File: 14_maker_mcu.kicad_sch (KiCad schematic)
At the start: 13 parts, among them J900 Maker MCU module socket, Pico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, J901 Exposed maker GPIO/power head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, J902 Maker SWD/debug header, SW900 Maker reset/RUN, SW901 Maker boot/user, U900 USBLC6-2P6 maker USB ESD

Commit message: Publish the current Ducktop2 design
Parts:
- added C902: 4.7u flash bulk, Capacitor_SMD:C_0402_1005Metric, symbol Device:C
- added C903: 100n flash local, Capacitor_SMD:C_0402_1005Metric, symbol Device:C
- added C904, C905, C906, C907, C908, C909, C910: 100n RP2350 3V3 local, Capacitor_SMD:C_0402_1005Metric, symbol Device:C
- added C911: 4.7u VREG input, Capacitor_SMD:C_0402_1005Metric, symbol Device:C
- added C912: 4.7u 1V1 output, Capacitor_SMD:C_0402_1005Metric, symbol Device:C
- added C917: 4.7u ADC_AVDD filter, Capacitor_SMD:C_0402_1005Metric, symbol Device:C
- added C918: 15p XIN load, Capacitor_SMD:C_0402_1005Metric, symbol Device:C
- added C919: 15p XOUT load, Capacitor_SMD:C_0402_1005Metric, symbol Device:C
- added C921: 10u 10V X7R TPS62821 output B, Capacitor_SMD:C_0603_1608Metric, symbol Device:C
- added C922: 100n ADC_VREF filter, Capacitor_SMD:C_0402_1005Metric, symbol Device:C
- added C923: 120p 50V C0G TPS62821 feed-forward, Capacitor_SMD:C_0603_1608Metric, symbol Device:C
- added C924: 100n 16V X7R 5V switch input, Capacitor_SMD:C_0603_1608Metric, symbol Device:C
- added C925: 100n 16V X7R 5V header output, Capacitor_SMD:C_0603_1608Metric, symbol Device:C
- added C926: 100n 16V X7R 3V3 switch input, Capacitor_SMD:C_0603_1608Metric, symbol Device:C
- added C927: 100n 16V X7R 3V3 header output, Capacitor_SMD:C_0603_1608Metric, symbol Device:C
- added C928: 100n maker USB switch local, Capacitor_SMD:C_0603_1608Metric, symbol Device:C
- added C930, C931, C932, C933: 100n maker header isolator local, Capacitor_SMD:C_0603_1608Metric, symbol Device:C
- added C934: 100n maker header supervisor local, Capacitor_SMD:C_0603_1608Metric, symbol Device:C
- added J902: TC2030 Cortex SWD: VTref/SWDIO/RUN/SWCLK/GND/NC, Connector:Tag-Connect_TC2030-IDC-NL_2x03_P1.27mm_Vertical, symbol Connector_Generic:Conn_01x06
- added L900: 470nH TDK TFM201610ALM-R47MTAA, ducktop2:TDK_TFM201610, symbol Device:L
- added L901: 3.3u AOTA-B201610S3R3-101-T (orientation critical), Inductor_SMD:L_Wuerth_PMFI-201610_PMCI-compatible, symbol Device:L
- added Q901: 2N7002 physical host-VBUS USB connect gate, Package_TO_SOT_SMD:SOT-23, symbol Q_NMOS_SOT23_GSD:Q_NMOS_SOT23_GSD
- added Q903: 2N7002 maker header isolation enable gate, Package_TO_SOT_SMD:SOT-23, symbol Q_NMOS_SOT23_GSD:Q_NMOS_SOT23_GSD
- added R902: 450k 1% TPS62821 feedback high, Resistor_SMD:R_0603_1608Metric, symbol Device:R
- added R903: 100k RP2350 SMPS power-save pull-down, Resistor_SMD:R_0402_1005Metric, symbol Device:R
- added R904: DNP 10k QSPI CS pull-up, Resistor_SMD:R_0402_1005Metric, symbol Device:R
- added R905: 1k BOOTSEL isolation, Resistor_SMD:R_0402_1005Metric, symbol Device:R
- added R906: 1k crystal damping, Resistor_SMD:R_0402_1005Metric, symbol Device:R
- added R908: 200R ADC reference filter, Resistor_SMD:R_0402_1005Metric, symbol Device:R
- added R909: 1R ADC input isolator, Resistor_SMD:R_0402_1005Metric, symbol Device:R
- added R910: 1k active-low host-connected sense series, Resistor_SMD:R_0402_1005Metric, symbol Device:R
- added R911: 100k maker host-disconnected pull-up, Resistor_SMD:R_0402_1005Metric, symbol Device:R
- added R916: 1k reset switch series, Resistor_SMD:R_0402_1005Metric, symbol Device:R
- added R917: 0R VTref sense link, Resistor_SMD:R_0402_1005Metric, symbol Device:R
- added R918: 100R SWDIO series, Resistor_SMD:R_0402_1005Metric, symbol Device:R
- added R919: 100R SWCLK series, Resistor_SMD:R_0402_1005Metric, symbol Device:R
- added R920: 100k 1% TPS62821 feedback low, Resistor_SMD:R_0603_1608Metric, symbol Device:R
- added R921: 88.7k 1% (262-342mA 5V header limit), Resistor_SMD:R_0603_1608Metric, symbol Device:R
- added R922: 226k 1% (101-142mA 3V3 header limit), Resistor_SMD:R_0603_1608Metric, symbol Device:R
- added R923: 100k maker header rails default-off, Resistor_SMD:R_0603_1608Metric, symbol Device:R
- added R924: 10k maker header shared fault pull-up, Resistor_SMD:R_0603_1608Metric, symbol Device:R
- added R925: 10k maker USB default-disconnect pull-up, Resistor_SMD:R_0402_1005Metric, symbol Device:R
- added R930: 47k maker header isolation default-off, Resistor_SMD:R_0402_1005Metric, symbol Device:R
- added R931: 10k maker header supervisor pull-up, Resistor_SMD:R_0402_1005Metric, symbol Device:R
- added R932, R933, R934, R935, R936, R937, R938, R939, R940, R941, R942, R943, R944, R945, R946, R947, R948, R949, R950, R951, R952, R953, R954, R955, R956, R957, R958, R959, R960, R961: 330R maker header fault limit, Resistor_SMD:R_0402_1005Metric, symbol Device:R
- added SW900: Maker reset/RUN, Button_Switch_SMD:SW_SPST_B3S-1000, symbol Switch:SW_Push
- added SW901: Maker BOOTSEL, Button_Switch_SMD:SW_SPST_B3S-1000, symbol Switch:SW_Push
- added U902: W25Q32RVXHJQ 32Mbit (4MiB), Package_SON:Winbond_USON-8-1EP_3x2mm_P0.5mm_EP0.2x1.6mm, symbol Memory_Flash:W25Q32JVZP
- added U903: TPS62821DLC 1A adjustable buck, Package_SON:Texas_VSON-HR-8_1.5x2mm_P0.5mm, symbol TPS62821DLC:TPS62821DLC
- added U904: TPS2553DDBVR 5V header, 300mA nominal, Package_TO_SOT_SMD:SOT-23-6, symbol TPS2553D:TPS2553D
- added U905: TPS2553DDBVR 3V3 header, 120mA nominal, Package_TO_SOT_SMD:SOT-23-6, symbol TPS2553D:TPS2553D
- added U906: TS3USB30EDGSR maker USB host-state isolation, Package_SO:TSSOP-10_3x3mm_P0.5mm, symbol Interface_USB:TS3USB30EDGSR
- added U910: SN74CB3T3245PWR maker header isolation bank 1, Package_SO:TSSOP-20_4.4x6.5mm_P0.65mm, symbol SN74CB3T3245:SN74CB3T3245
- added U911: SN74CB3T3245PWR maker header isolation bank 2, Package_SO:TSSOP-20_4.4x6.5mm_P0.65mm, symbol SN74CB3T3245:SN74CB3T3245
- added U912: SN74CB3T3245PWR maker header isolation bank 3, Package_SO:TSSOP-20_4.4x6.5mm_P0.65mm, symbol SN74CB3T3245:SN74CB3T3245
- added U913: SN74CB3T3245PWR maker header isolation bank 4, Package_SO:TSSOP-20_4.4x6.5mm_P0.65mm, symbol SN74CB3T3245:SN74CB3T3245
- added U914: TPD4E05U06DQAR maker header ESD bank 1, Package_SON:USON-10_2.5x1.0mm_P0.5mm, symbol Power_Protection:TPD4E05U06DQA
- added U915: TPD4E05U06DQAR maker header ESD bank 2, Package_SON:USON-10_2.5x1.0mm_P0.5mm, symbol Power_Protection:TPD4E05U06DQA
- added U916: TPD4E05U06DQAR maker header ESD bank 3, Package_SON:USON-10_2.5x1.0mm_P0.5mm, symbol Power_Protection:TPD4E05U06DQA
- added U917: TPD4E05U06DQAR maker header ESD bank 4, Package_SON:USON-10_2.5x1.0mm_P0.5mm, symbol Power_Protection:TPD4E05U06DQA
- added U918: TPD4E05U06DQAR maker header ESD bank 5, Package_SON:USON-10_2.5x1.0mm_P0.5mm, symbol Power_Protection:TPD4E05U06DQA
- added U919: TPD4E05U06DQAR maker header ESD bank 6, Package_SON:USON-10_2.5x1.0mm_P0.5mm, symbol Power_Protection:TPD4E05U06DQA
- added U920: TPD4E05U06DQAR maker header ESD bank 7, Package_SON:USON-10_2.5x1.0mm_P0.5mm, symbol Power_Protection:TPD4E05U06DQA
- added U921: TPD4E05U06DQAR maker header ESD bank 8, Package_SON:USON-10_2.5x1.0mm_P0.5mm, symbol Power_Protection:TPD4E05U06DQA
- added U922: TLV803EA29RDBZR maker header rail supervisor, Package_TO_SOT_SMD:SOT-23-3, symbol TLV803EA29RDBZR:TLV803EA29RDBZR
- added Y900: Abracon ABM8-272-T3 12MHz, Crystal:Crystal_SMD_3225-4Pin_3.2x2.5mm, symbol Device:Crystal_GND24
- C900: value 10u maker 5V bulk -> 4.7u 6.3V X7R TPS62821 input; footprint Capacitor_SMD:C_1206_3216Metric -> Capacitor_SMD:C_0603_1608Metric; MPN (none) -> JMK107BB7475MA-T; Manufacturer (none) -> Taiyo Yuden
- C901: value 1u maker 3V3 local -> 10u 10V X7R TPS62821 output A; footprint Capacitor_SMD:C_0805_2012Metric -> Capacitor_SMD:C_0603_1608Metric; MPN (none) -> GRM188Z71A106MA73D; Manufacturer (none) -> Murata
- C913: renamed from SW900; value Maker reset/RUN -> 4.7u VREG_AVDD; footprint Button_Switch_SMD:SW_SPST_B3S-1000 -> Capacitor_SMD:C_0402_1005Metric; symbol Switch:SW_Push -> Device:C
- C914: renamed from R903; value 100k BOOT pull-up -> 100n DVDD A; footprint Resistor_SMD:R_0603_1608Metric -> Capacitor_SMD:C_0402_1005Metric; symbol Device:R -> Device:C
- C915: renamed from SW901; value Maker boot/user -> 100n DVDD B; footprint Button_Switch_SMD:SW_SPST_B3S-1000 -> Capacitor_SMD:C_0402_1005Metric; symbol Switch:SW_Push -> Device:C
- C916: renamed from J902; value Maker SWD/debug header -> 100n DVDD C; footprint Connector_PinHeader_2.54mm:PinHeader_1x04_P2.54mm_Vertical -> Capacitor_SMD:C_0402_1005Metric; symbol Connector_Generic:Conn_01x04 -> Device:C
- F900: value 500mA maker 5V fuse/polyfuse -> 1.1A hold PPTC Littelfuse 1206L110/16WR; MPN (none) -> 1206L110/16WR; Manufacturer (none) -> Littelfuse
- J901: value Exposed maker GPIO/power header -> JST PUD 2x20 protected maker GPIO/power; NOT A PI HAT; footprint Connector_PinHeader_2.54mm:PinHeader_2x20_P2.54mm_Vertical -> Connector_JST:JST_PUD_B40B-PUDSS_2x20_P2.00mm_Vertical; Contacts (none) -> SPUD-001T-P0.5 or SPUD-002T-P0.5; InterfaceWarning (none) -> NOT_RASPBERRY_PI_HAT_PINOUT_OR_PITCH; MPN (none) -> B40B-PUDSS; Manufacturer (none) -> JST; MatingHousing (none) -> PUDP-40V-S
- R900: value 22R maker USB DP series -> 27R USB DP termination; footprint Resistor_SMD:R_0603_1608Metric -> Resistor_SMD:R_0402_1005Metric
- R901: value 22R maker USB DM series -> 27R USB DM termination; footprint Resistor_SMD:R_0603_1608Metric -> Resistor_SMD:R_0402_1005Metric
- R907: renamed from R902; value 100k RUN pull-up -> 33R VREG_AVDD filter; footprint Resistor_SMD:R_0603_1608Metric -> Resistor_SMD:R_0402_1005Metric
- U900: MPN (none) -> USBLC6-2P6; Manufacturer (none) -> STMicroelectronics
- U901: renamed from J900; value Maker MCU module socket, Pico/Arduino-class -> RP2350A; footprint Connector_PinHeader_2.54mm:PinHeader_2x20_P2.54mm_Vertical -> Package_DFN_QFN:QFN-60-1EP_7x7mm_P0.4mm_EP3.4x3.4mm_ThermalVias; symbol Connector_Generic:Conn_02x20_Odd_Even -> MCU_RaspberryPi:RP2350A; MPN (none) -> RP2350A (A4 stepping); Manufacturer (none) -> Raspberry Pi
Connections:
- net GND: now also C914.2, C916.2, J901.3 (Pin_3), J901.33 (Pin_33), J901.34 (Pin_34), U901.47 (VREG_PGND), U901.61 (GND), C902.2, C903.2, C904.2, C905.2, C906.2, C907.2, C908.2, C909.2, C910.2, C911.2, C912.2, C917.2, C918.2, C919.2, C921.2, C922.2, C924.2, C925.2, C926.2, C927.2, C928.2, C930.2, C931.2, C932.2, C933.2, C934.2, J902.5 (Pin_5), Q901.2 (S), Q903.2 (S), R903.2, R916.2, R920.2, R921.2, R922.2, R923.2, SW901.2, U902.4 (GND), U902.9 (EP), U903.3 (AGND), U903.5 (PGND), U904.2 (GND), U905.2 (GND), U906.1 (S), U906.5 (GND), U910.10 (GND), U911.10 (GND), U912.10 (GND), U913.10 (GND), U914.3 (GND), U914.8 (GND), U915.3 (GND), U915.8 (GND), U916.3 (GND), U916.8 (GND), U917.3 (GND), U917.8 (GND), U918.3 (GND), U918.8 (GND), U919.3 (GND), U919.8 (GND), U920.3 (GND), U920.8 (GND), U921.3 (GND), U921.8 (GND), U922.2 (GND), Y900.2 (G), Y900.4 (G); no longer C916.1 (Pin_1), U901.1 (Pin_1), U901.38 (Pin_38), U901.40 (Pin_40)
- net MAKER_ADC0: now also U901.40 (GPIO26/ADC0), U913.5 (A4); no longer J901.35 (Pin_35), U901.35 (Pin_35)
- net MAKER_ADC1: now also U901.41 (GPIO27/ADC1), U913.6 (A5); no longer J901.36 (Pin_36), U901.36 (Pin_36)
- net MAKER_ADC2: now also U901.42 (GPIO28/ADC2), U913.7 (A6); no longer J901.39 (Pin_39), U901.39 (Pin_39)
- net MAKER_BOOT_N: now also R905.2, SW901.1, U910.2 (A1); no longer C914.2, C915.1, J901.5 (Pin_5), U901.5 (Pin_5)
- net MAKER_GPIO0: now also U901.7 (GPIO4), U911.6 (A5); no longer J901.17 (Pin_17), U901.17 (Pin_17)
- net MAKER_GPIO1: now also U901.8 (GPIO5), U911.7 (A6); no longer J901.18 (Pin_18), U901.18 (Pin_18)
- net MAKER_GPIO10: now also U901.18 (GPIO14), U912.8 (A7); no longer J901.27 (Pin_27), U901.27 (Pin_27)
- net MAKER_GPIO11: now also U901.19 (GPIO15), U912.9 (A8); no longer J901.28 (Pin_28), U901.28 (Pin_28)
- net MAKER_GPIO12: now also U901.32 (GPIO20), U913.2 (A1); no longer J901.29 (Pin_29), U901.29 (Pin_29)
- net MAKER_GPIO13: now also U901.33 (GPIO21), U913.3 (A2); no longer J901.30 (Pin_30), U901.30 (Pin_30)
- net MAKER_GPIO14: now also U901.34 (GPIO22), U913.4 (A3); no longer J901.31 (Pin_31), U901.31 (Pin_31)
- net MAKER_GPIO2: now also U901.9 (GPIO6), U911.8 (A7); no longer J901.19 (Pin_19), U901.19 (Pin_19)
- net MAKER_GPIO3: now also U901.10 (GPIO7), U911.9 (A8); no longer J901.20 (Pin_20), U901.20 (Pin_20)
- net MAKER_GPIO4: now also U901.12 (GPIO8), U912.2 (A1); no longer J901.21 (Pin_21), U901.21 (Pin_21)
- net MAKER_GPIO5: now also U901.13 (GPIO9), U912.3 (A2); no longer J901.22 (Pin_22), U901.22 (Pin_22)
- net MAKER_GPIO6: now also U901.14 (GPIO10), U912.4 (A3); no longer J901.23 (Pin_23), U901.23 (Pin_23)
- net MAKER_GPIO7: now also U901.15 (GPIO11), U912.5 (A4); no longer J901.24 (Pin_24), U901.24 (Pin_24)
- net MAKER_GPIO8: now also U901.16 (GPIO12), U912.6 (A5); no longer J901.25 (Pin_25), U901.25 (Pin_25)
- net MAKER_GPIO9: now also U901.17 (GPIO13), U912.7 (A6); no longer J901.26 (Pin_26), U901.26 (Pin_26)
- net MAKER_I2C_SCL: now also U901.5 (GPIO3), U910.8 (A7); no longer J901.11 (Pin_11), U901.11 (Pin_11)
- net MAKER_I2C_SDA: now also U901.4 (GPIO2), U910.9 (A8); no longer J901.12 (Pin_12), U901.12 (Pin_12)
- net MAKER_RUN_N: now also U901.26 (RUN), J902.3 (Pin_3), SW900.1, U910.3 (A2); no longer C913.1, J901.6 (Pin_6), R907.2, U901.6 (Pin_6)
- net MAKER_SPI_CS_N: now also U901.28 (GPIO17), U911.5 (A4); no longer J901.16 (Pin_16), U901.16 (Pin_16)
- net MAKER_SPI_MISO: now also U901.27 (GPIO16), U911.3 (A2); no longer J901.14 (Pin_14), U901.14 (Pin_14)
- net MAKER_SPI_MOSI: now also U901.31 (GPIO19), U911.4 (A3); no longer J901.15 (Pin_15), U901.15 (Pin_15)
- net MAKER_SPI_SCK: now also U901.29 (GPIO18), U911.2 (A1); no longer J901.13 (Pin_13), U901.13 (Pin_13)
- net MAKER_SWCLK: now also J902.4 (Pin_4), R919.2, U910.5 (A4); no longer C916.4 (Pin_4), J901.8 (Pin_8), U901.8 (Pin_8)
- net MAKER_SWDIO: now also J902.2 (Pin_2), R918.2, U910.4 (A3); no longer C916.3 (Pin_3), J901.7 (Pin_7), U901.7 (Pin_7)
- net MAKER_UART_RX: now also U901.3 (GPIO1), U910.7 (A6); no longer J901.10 (Pin_10), U901.10 (Pin_10)
- net MAKER_UART_TX: now also U901.2 (GPIO0), U910.6 (A5); no longer J901.9 (Pin_9), U901.9 (Pin_9)
- net MAKER_USB_DM: now also U900.3 (I/O2), U900.4 (I/O2), U906.8 (D1-); no longer R901.1
- net MAKER_USB_DP: now also U900.1 (I/O1), U900.6 (I/O1), U906.2 (D1+); no longer R900.1
- removed net MAKER_3V3: C901.1, C914.1, C916.2 (Pin_2), J901.37 (Pin_37), R907.1, U901.37 (Pin_37)
- net MAKER_5V renamed MAKER_5V_CORE
- net MAKER_5V_CORE: now also C924.1, U903.1 (EN), U903.7 (VIN), U904.1 (IN); no longer J901.2 (Pin_2), U901.2 (Pin_2)
- net MAKER_GPIO15: no longer names the net of J901.32 (Pin_32)
- net MAKER_GPIO15: no longer U901.32 (Pin_32)
- removed net MAKER_GPIO16: J901.33 (Pin_33), U901.33 (Pin_33)
- removed net MAKER_GPIO17: J901.34 (Pin_34), U901.34 (Pin_34)
- removed net MAKER_USB_CONN_DM: J901.3 (Pin_3), R901.2, U900.3 (I/O2), U900.4 (I/O2), U901.3 (Pin_3)
- removed net MAKER_USB_CONN_DP: J901.4 (Pin_4), R900.2, U900.1 (I/O1), U900.6 (I/O1), U901.4 (Pin_4)
- new net INTERNAL_USB_VBUS_VALID: Q901.1 (G)
- new net J901_3V3_OUT: C927.1, J901.37 (Pin_37), J901.4 (Pin_4), U905.6 (OUT)
- new net J901_5V_OUT: C925.1, J901.2 (Pin_2), U904.6 (OUT)
- new net J901_MAKER_ADC0: J901.35 (Pin_35), R959.2, U920.5 (D2-)
- new net J901_MAKER_ADC0_ISO: R959.1, U913.15 (B4)
- new net J901_MAKER_ADC1: J901.36 (Pin_36), R960.2, U921.1 (D1+)
- new net J901_MAKER_ADC1_ISO: R960.1, U913.14 (B5)
- new net J901_MAKER_ADC2: J901.39 (Pin_39), R961.2, U921.2 (D1-)
- new net J901_MAKER_ADC2_ISO: R961.1, U913.13 (B6)
- new net J901_MAKER_BOOT_N: J901.5 (Pin_5), R932.2, U914.1 (D1+)
- new net J901_MAKER_BOOT_N_ISO: R932.1, U910.18 (B1)
- new net J901_MAKER_GPIO0: J901.17 (Pin_17), R944.2, U917.1 (D1+)
- new net J901_MAKER_GPIO0_ISO: R944.1, U911.14 (B5)
- new net J901_MAKER_GPIO1: J901.18 (Pin_18), R945.2, U917.2 (D1-)
- new net J901_MAKER_GPIO10: J901.27 (Pin_27), R954.2, U919.4 (D2+)
- new net J901_MAKER_GPIO10_ISO: R954.1, U912.12 (B7)
- new net J901_MAKER_GPIO11: J901.28 (Pin_28), R955.2, U919.5 (D2-)
- new net J901_MAKER_GPIO11_ISO: R955.1, U912.11 (B8)
- new net J901_MAKER_GPIO12: J901.29 (Pin_29), R956.2, U920.1 (D1+)
- new net J901_MAKER_GPIO12_ISO: R956.1, U913.18 (B1)
- new net J901_MAKER_GPIO13: J901.30 (Pin_30), R957.2, U920.2 (D1-)
- new net J901_MAKER_GPIO13_ISO: R957.1, U913.17 (B2)
- new net J901_MAKER_GPIO14: J901.31 (Pin_31), R958.2, U920.4 (D2+)
- new net J901_MAKER_GPIO14_ISO: R958.1, U913.16 (B3)
- new net J901_MAKER_GPIO1_ISO: R945.1, U911.13 (B6)
- new net J901_MAKER_GPIO2: J901.19 (Pin_19), R946.2, U917.4 (D2+)
- new net J901_MAKER_GPIO2_ISO: R946.1, U911.12 (B7)
- new net J901_MAKER_GPIO3: J901.20 (Pin_20), R947.2, U917.5 (D2-)
- new net J901_MAKER_GPIO3_ISO: R947.1, U911.11 (B8)
- new net J901_MAKER_GPIO4: J901.21 (Pin_21), R948.2, U918.1 (D1+)
- new net J901_MAKER_GPIO4_ISO: R948.1, U912.18 (B1)
- new net J901_MAKER_GPIO5: J901.22 (Pin_22), R949.2, U918.2 (D1-)
- new net J901_MAKER_GPIO5_ISO: R949.1, U912.17 (B2)
- new net J901_MAKER_GPIO6: J901.23 (Pin_23), R950.2, U918.4 (D2+)
- new net J901_MAKER_GPIO6_ISO: R950.1, U912.16 (B3)
- new net J901_MAKER_GPIO7: J901.24 (Pin_24), R951.2, U918.5 (D2-)
- new net J901_MAKER_GPIO7_ISO: R951.1, U912.15 (B4)
- new net J901_MAKER_GPIO8: J901.25 (Pin_25), R952.2, U919.1 (D1+)
- new net J901_MAKER_GPIO8_ISO: R952.1, U912.14 (B5)
- new net J901_MAKER_GPIO9: J901.26 (Pin_26), R953.2, U919.2 (D1-)
- new net J901_MAKER_GPIO9_ISO: R953.1, U912.13 (B6)
- new net J901_MAKER_I2C_SCL: J901.11 (Pin_11), R938.2, U915.4 (D2+)
- new net J901_MAKER_I2C_SCL_ISO: R938.1, U910.12 (B7)
- new net J901_MAKER_I2C_SDA: J901.12 (Pin_12), R939.2, U915.5 (D2-)
- new net J901_MAKER_I2C_SDA_ISO: R939.1, U910.11 (B8)
- new net J901_MAKER_RUN_N: J901.6 (Pin_6), R933.2, U914.2 (D1-)
- new net J901_MAKER_RUN_N_ISO: R933.1, U910.17 (B2)
- new net J901_MAKER_SPI_CS_N: J901.16 (Pin_16), R943.2, U916.5 (D2-)
- new net J901_MAKER_SPI_CS_N_ISO: R943.1, U911.15 (B4)
- new net J901_MAKER_SPI_MISO: J901.14 (Pin_14), R941.2, U916.2 (D1-)
- new net J901_MAKER_SPI_MISO_ISO: R941.1, U911.17 (B2)
- new net J901_MAKER_SPI_MOSI: J901.15 (Pin_15), R942.2, U916.4 (D2+)
- new net J901_MAKER_SPI_MOSI_ISO: R942.1, U911.16 (B3)
- new net J901_MAKER_SPI_SCK: J901.13 (Pin_13), R940.2, U916.1 (D1+)
- new net J901_MAKER_SPI_SCK_ISO: R940.1, U911.18 (B1)
- new net J901_MAKER_SWCLK: J901.8 (Pin_8), R935.2, U914.5 (D2-)
- new net J901_MAKER_SWCLK_ISO: R935.1, U910.15 (B4)
- new net J901_MAKER_SWDIO: J901.7 (Pin_7), R934.2, U914.4 (D2+)
- new net J901_MAKER_SWDIO_ISO: R934.1, U910.16 (B3)
- new net J901_MAKER_UART_RX: J901.10 (Pin_10), R937.2, U915.2 (D1-)
- new net J901_MAKER_UART_RX_ISO: R937.1, U910.13 (B6)
- new net J901_MAKER_UART_TX: J901.9 (Pin_9), R936.2, U915.1 (D1+)
- new net J901_MAKER_UART_TX_ISO: R936.1, U910.14 (B5)
- new net MAKER_1V1: C912.1, C914.1, C915.1, C916.1, L901.1, U901.23 (DVDD), U901.39 (DVDD), U901.50 (VREG_FB), U901.6 (DVDD)
- new net MAKER_3V3_CORE: C901.1, C902.1, C903.1, C904.1, C905.1, C906.1, C907.1, C908.1, C909.1, C910.1, C911.1, C921.1, C923.1, C926.1, C928.1, C930.1, C931.1, C932.1, C933.1, C934.1, L900.2, R902.1, R904.1, R907.1, R908.1, R911.1, R917.1, R924.1, R925.1, R930.1, R931.1, U901.1 (IOVDD), U901.11 (IOVDD), U901.20 (IOVDD), U901.30 (IOVDD), U901.38 (IOVDD), U901.45 (IOVDD), U901.49 (VREG_VIN), U901.53 (USB_OTP_VDD), U901.54 (QSPI_IOVDD), U902.8 (VCC), U905.1 (IN), U906.10 (VCC), U910.20 (VCC), U911.20 (VCC), U912.20 (VCC), U913.20 (VCC), U922.3 (VDD)
- new net MAKER_3V3_FB: C923.2, R902.2, R920.1, U903.2 (FB)
- new net MAKER_3V3_ILIM: R922.1, U905.5 (ILIM)
- new net MAKER_3V3_SW: L900.1, U903.6 (SW)
- new net MAKER_5V_ILIM: R921.1, U904.5 (ILIM)
- new net MAKER_ADC_AVDD: C917.1, R909.2, U901.44 (ADC_AVDD)
- new net MAKER_ADC_VREF: C922.1, R908.2, R909.1
- new net MAKER_HEADER_OE_N: Q903.3 (D), R930.2, U910.19 (~{OE}), U911.19 (~{OE}), U912.19 (~{OE}), U913.19 (~{OE})
- new net MAKER_HEADER_VALID: Q903.1 (G), R931.2, U922.1 (RESETz)
- new net MAKER_HOST_ACTIVE_N: R910.2, R911.2, U901.36 (GPIO24)
- new net MAKER_PWR_EN: R923.1, U901.43 (GPIO29/ADC3), U904.3 (EN), U905.3 (EN)
- new net MAKER_PWR_FAULT_N: R924.2, U901.37 (GPIO25), U904.4 (~{FAULT}), U905.4 (~{FAULT})
- new net MAKER_QSPI_SCLK: U901.56 (QSPI_SCLK), U902.6 (CLK)
- new net MAKER_QSPI_SD0: U901.57 (QSPI_SD0), U902.5 (DI/IO_{0})
- new net MAKER_QSPI_SD1: U901.59 (QSPI_SD1), U902.2 (DO/IO_{1})
- new net MAKER_QSPI_SD2: U901.58 (QSPI_SD2), U902.3 (~{WP}/IO_{2})
- new net MAKER_QSPI_SD3: U901.55 (QSPI_SD3), U902.7 (~{HOLD}/~{RESET}/IO_{3})
- new net MAKER_QSPI_SS: R904.2, R905.1, U901.60 (~{QSPI_SS}), U902.1 (~{CS})
- new net MAKER_RUN_SW: R916.1, SW900.2
- new net MAKER_SMPS_PS: R903.1, U901.35 (GPIO23)
- new net MAKER_SWCLK_MCU: R919.1, U901.24 (SWCLK)
- new net MAKER_SWDIO_MCU: R918.1, U901.25 (SWDIO)
- new net MAKER_SWD_VTREF: J902.1 (Pin_1), R917.2
- new net MAKER_USB_DM_MCU: R901.2, U901.51 (USB_DM)
- new net MAKER_USB_DP_MCU: R900.2, U901.52 (USB_DP)
- new net MAKER_USB_ISO_DM: R901.1, U906.6 (D-)
- new net MAKER_USB_ISO_DP: R900.1, U906.4 (D+)
- new net MAKER_USB_OE_N: Q901.3 (D), R910.1, R925.2, U906.9 (~{OE})
- new net MAKER_VREG_AVDD: C913.1, R907.2, U901.46 (VREG_AVDD)
- new net MAKER_VREG_LX: L901.2, U901.48 (VREG_LX)
- new net MAKER_XIN: C918.1, U901.21 (XIN), Y900.1
- new net MAKER_XOUT: R906.2, U901.22 (XOUT)
- new net MAKER_XTAL_R: C919.1, R906.1, Y900.3
- no-connect marks 0 -> 48
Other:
- note added: "== Direct internal USB, Pico utility GPIO, reset/boot, and SWD =="
- note added: "== Integrated RP2350 maker controller (Pico 2 architecture, no module/cable) =="
- note added: "== Maker core rails and reverse-blocked header power outputs =="
- note added: "== Protected user-facing maker GPIO header =="
- note added: "== RP2350 12MHz clock and internal 1.1V switcher =="
- note added: "== RP2350A and 4MB QSPI flash =="
- note added: "J901 is keyed/latching JST PUD 2.00mm and NOT Pi-HAT compatible. U910-U913 isolate and tolerate 5V at the connector; 5.5V-standoff U914-U921 provide connector-side ESD."
- note added: "Keep Y900/R906/C918/C919 tight to XIN/XOUT. Keep QSPI traces short; place C902/C903 at U902."
- note added: "LAYOUT-CRITICAL NOTES:"
- note added: "No Pico module, Micro-USB receptacle, or internal USB cable is used. The integrated RP2350 is the USB device."
- note added: "Place L901/C911/C912/C913/R907 exactly around U901 per Raspberry Pi RP2350 guidance; keep LX copper tiny."
- note added: "Place R900/R901 at U901 USB pins and U906 in the short Mu path; route both pairs as 90-ohm differential over uninterrupted ground."
- note added: "Power, flash, crystal, BOOTSEL, reset, SWD, ADC filtering, and decoupling follow Raspberry Pi Pico 2 guidance."
- note added: "R932-R961 are 330R fault-limit resistors. Digital outputs are 3.3V only; use external I2C pull-ups >=4.7k and initially keep SPI/SWD <=10MHz."
- note added: "The ADC reference remains internal. J901 ADC precision range is 0-3.0V; 5.5V tolerance is for accidental input only and must be validated, not treated as an ADC range."
- note added: "The Mu USB2_P7 pair reaches U901 through a default-disconnected host-state switch. J901 is the external tinkering header, not a module socket."
- note added: "U906 defaults disconnected and connects only after physical INTERNAL_USB_VBUS is valid. The maker cannot wake S3; firmware reinitializes USB when MAKER_HOST_ACTIVE_N falls."
- note added: "U922/Q903 hold all 30 signals disconnected until MAKER_3V3_CORE is valid. Header power rails separately default OFF and are current-limited."
- note removed: "== Maker MCU module/mezzanine interface =="
- note removed: "== Power, USB, and bring-up controls =="
- note removed: "== User maker MCU bay: Arduino/Pico-class sandbox controller =="
- note removed: "== User-facing maker GPIO header =="
- note removed: "If a specific Pico/RP2350/Arduino module is chosen later, replace J900 pinout/footprint with that exact module."
- note removed: "MAKER_USB_DP/DM come from Mu USB2_P7 so the host OS sees this as a normal USB dev board."
- note removed: "Module is host-programmable over Mu USB2_P7 and exposes 3.3V GPIO on a user header."
- note removed: "NOTES:"
- note removed: "This is intentionally separate from the laptop EC so experiments cannot break keyboard/power/fan control."
- note removed: "Treat J900 as the internal programmable module interface; J901 exposes the same sandbox pins for tinkering."
- note removed: "Use 3.3V GPIO only. MAKER_5V is fused and intended for the module/input side, not arbitrary high-current loads."
- moved on the sheet: R907

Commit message: Assign 327 BOM MPNs across 11 schematic sheets (370→43 gaps)
Closes 370 BOM procurement gaps by assigning Yageo resistor and Murata
capacitor MPNs to all passive components in the project's 11 schematic
sheets. 43 intentional holds remain for design-review items (crystal
loads, audio AC-coupling, VCAP, C0G timing, maker MCU 4.7u 0402s).

Key changes:
- 205 resistors assigned (Yageo RC0603/RT0603 series)
- 124 capacitors assigned (Murata GRM series, matching footprint body size)
- Fixed C183: 4.7u MPN→1u (GRM21BR71A105KA01L)
- Fixed C795/C840: upgraded to 50V rating (GRM21BR71H105KA12L)
- Generated fresh inventory: 1173 components, 43 remaining gaps
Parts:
- C903, C904, C905, C906, C907, C908, C909, C910, C914, C915, C916, C922: MPN (none) -> GRM155R71A104KA01D; Manufacturer (none) -> Murata
- C928, C930, C931, C932, C933, C934: MPN (none) -> GRM188R71H104KA93D; Manufacturer (none) -> Murata
- R900, R901: MPN (none) -> RC0402FR-0727RL; Manufacturer (none) -> Yageo
- R902: MPN (none) -> RC0603FR-07450KL; Manufacturer (none) -> Yageo
- R903, R911: MPN (none) -> RC0402FR-07100KL; Manufacturer (none) -> Yageo
- R905, R906, R910, R916: MPN (none) -> RC0402FR-071KL; Manufacturer (none) -> Yageo
- R907: MPN (none) -> RC0402FR-0733RL; Manufacturer (none) -> Yageo
- R908: MPN (none) -> RC0402FR-07200RL; Manufacturer (none) -> Yageo
- R909: MPN (none) -> RC0402FR-071RL; Manufacturer (none) -> Yageo
- R917: MPN (none) -> RC0402FR-070RL; Manufacturer (none) -> Yageo
- R918, R919: MPN (none) -> RC0402FR-07100RL; Manufacturer (none) -> Yageo
- R920, R923: MPN (none) -> RC0603FR-07100KL; Manufacturer (none) -> Yageo
- R921: MPN (none) -> RC0603FR-0788K7L; Manufacturer (none) -> Yageo
- R922: MPN (none) -> RC0603FR-07226KL; Manufacturer (none) -> Yageo
- R924: MPN (none) -> RC0603FR-0710KL; Manufacturer (none) -> Yageo
- R925, R931: MPN (none) -> RC0402FR-0710KL; Manufacturer (none) -> Yageo

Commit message: Regenerate child schematics to sync with current generators
The committed .kicad_sch carried stale embedded Manufacturer/MPN properties from the old per-component BOM approach (MPNs now live in verification/BOM_MPN_ASSIGNMENTS.md). Regenerating from the current generators strips those stale properties and clears the pre-existing Generated-source identity release-check failure. No connectivity change; ERC still 0 errors / 27 intentional warnings; schematic closure 1569/0.
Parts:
- C903, C904, C905, C906, C907, C908, C909, C910, C914, C915, C916, C922: MPN GRM155R71A104KA01D -> (none); Manufacturer Murata -> (none)
- C928, C930, C931, C932, C933, C934: MPN GRM188R71H104KA93D -> (none); Manufacturer Murata -> (none)
- R900, R901: MPN RC0402FR-0727RL -> (none); Manufacturer Yageo -> (none)
- R902: MPN RC0603FR-07450KL -> (none); Manufacturer Yageo -> (none)
- R903, R911: MPN RC0402FR-07100KL -> (none); Manufacturer Yageo -> (none)
- R905, R906, R910, R916: MPN RC0402FR-071KL -> (none); Manufacturer Yageo -> (none)
- R907: MPN RC0402FR-0733RL -> (none); Manufacturer Yageo -> (none)
- R908: MPN RC0402FR-07200RL -> (none); Manufacturer Yageo -> (none)
- R909: MPN RC0402FR-071RL -> (none); Manufacturer Yageo -> (none)
- R917: MPN RC0402FR-070RL -> (none); Manufacturer Yageo -> (none)
- R918, R919: MPN RC0402FR-07100RL -> (none); Manufacturer Yageo -> (none)
- R920, R923: MPN RC0603FR-07100KL -> (none); Manufacturer Yageo -> (none)
- R921: MPN RC0603FR-0788K7L -> (none); Manufacturer Yageo -> (none)
- R922: MPN RC0603FR-07226KL -> (none); Manufacturer Yageo -> (none)
- R924: MPN RC0603FR-0710KL -> (none); Manufacturer Yageo -> (none)
- R925, R931: MPN RC0402FR-0710KL -> (none); Manufacturer Yageo -> (none)

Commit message: Stamp generation-time BOM catalog; close 378 procurement gaps
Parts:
- C902, C911, C912, C913, C917: MPN (none) -> GRM155R61A475KE15; Manufacturer (none) -> Murata
- C903, C904, C905, C906, C907, C908, C909, C910, C914, C915, C916, C922: MPN (none) -> GRM155R71A104KA01D; Manufacturer (none) -> Murata
- C918, C919: MPN (none) -> GRM1555C1H150JA01; Manufacturer (none) -> Murata
- C928, C930, C931, C932, C933, C934: MPN (none) -> GRM188R71H104KA93D; Manufacturer (none) -> Murata
- R900, R901: MPN (none) -> RC0402FR-0727RL; Manufacturer (none) -> Yageo
- R902: MPN (none) -> RC0603FR-07450KL; Manufacturer (none) -> Yageo
- R903, R911: MPN (none) -> RC0402FR-07100KL; Manufacturer (none) -> Yageo
- R905, R906, R910, R916: MPN (none) -> RC0402FR-071KL; Manufacturer (none) -> Yageo
- R907: MPN (none) -> RC0402FR-0733RL; Manufacturer (none) -> Yageo
- R908: MPN (none) -> RC0402FR-07200RL; Manufacturer (none) -> Yageo
- R909: MPN (none) -> RC0402FR-071RL; Manufacturer (none) -> Yageo
- R917: MPN (none) -> RC0402FR-070RL; Manufacturer (none) -> Yageo
- R918, R919: MPN (none) -> RC0402FR-07100RL; Manufacturer (none) -> Yageo
- R920, R923: MPN (none) -> RC0603FR-07100KL; Manufacturer (none) -> Yageo
- R921: MPN (none) -> RC0603FR-0788K7L; Manufacturer (none) -> Yageo
- R922: MPN (none) -> RC0603FR-07226KL; Manufacturer (none) -> Yageo
- R924: MPN (none) -> RC0603FR-0710KL; Manufacturer (none) -> Yageo
- R925, R931: MPN (none) -> RC0402FR-0710KL; Manufacturer (none) -> Yageo

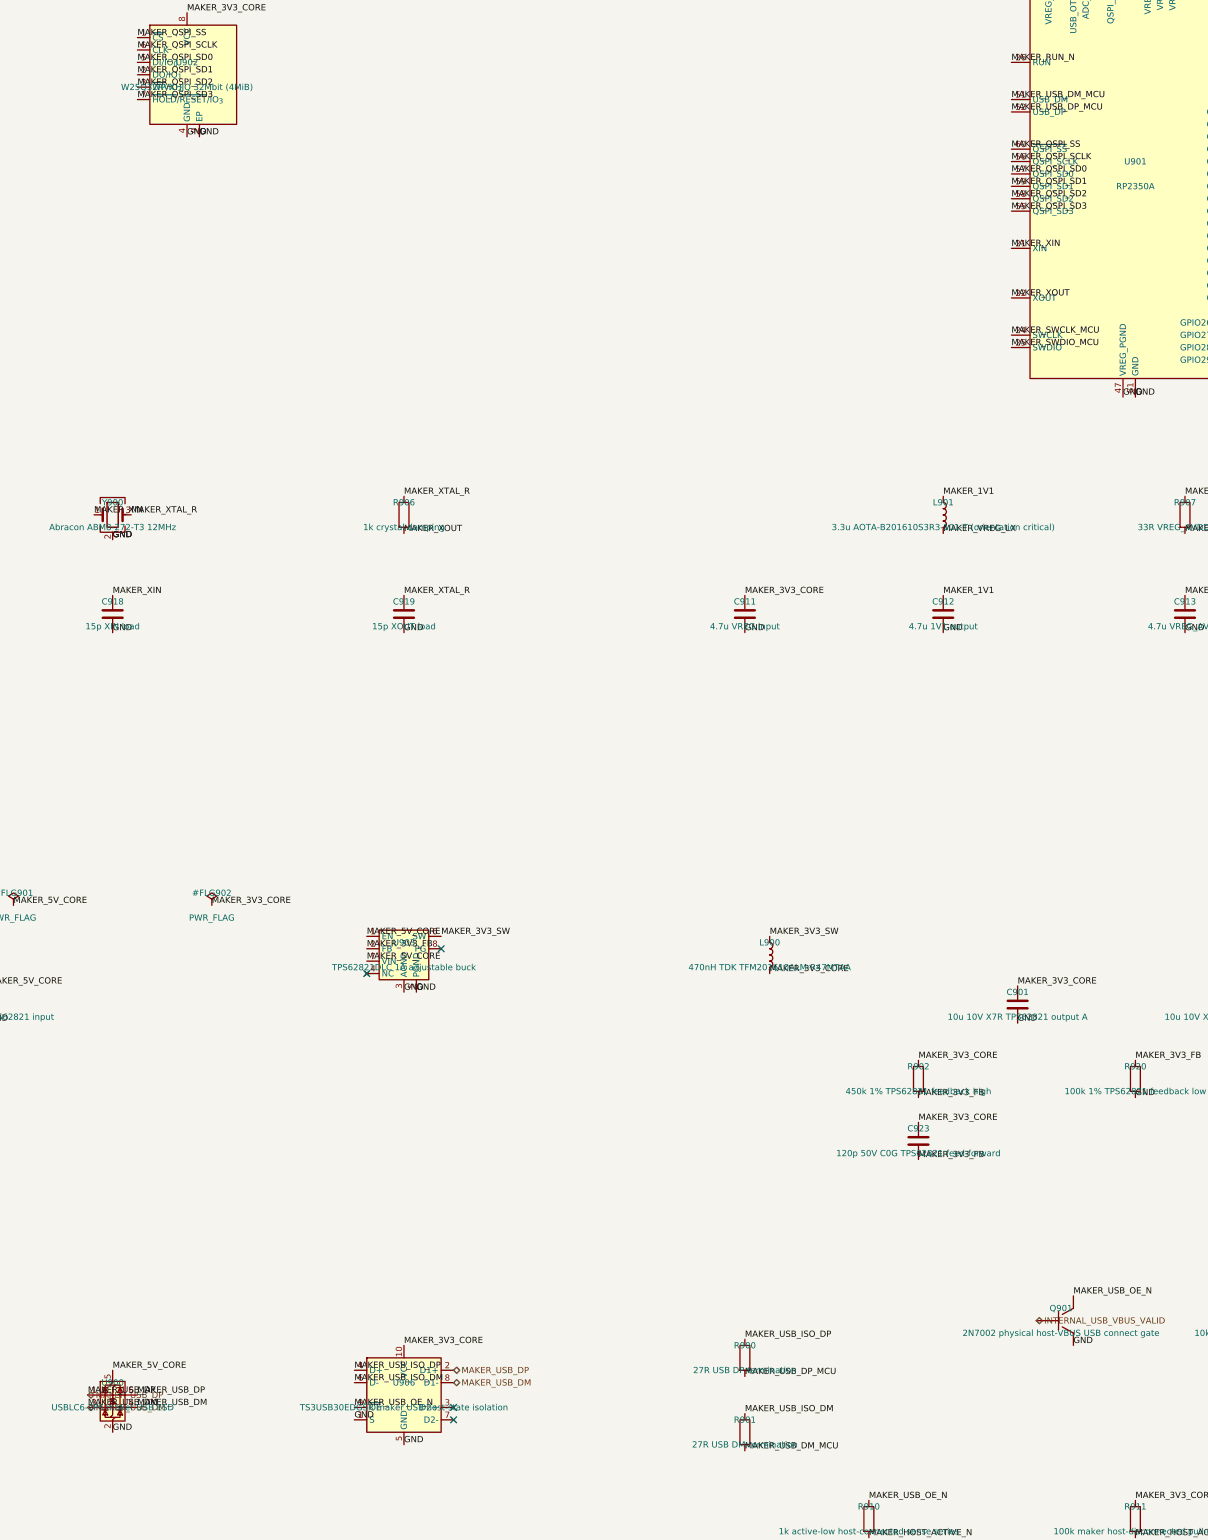
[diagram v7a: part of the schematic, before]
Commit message: get the main boards ready for routing
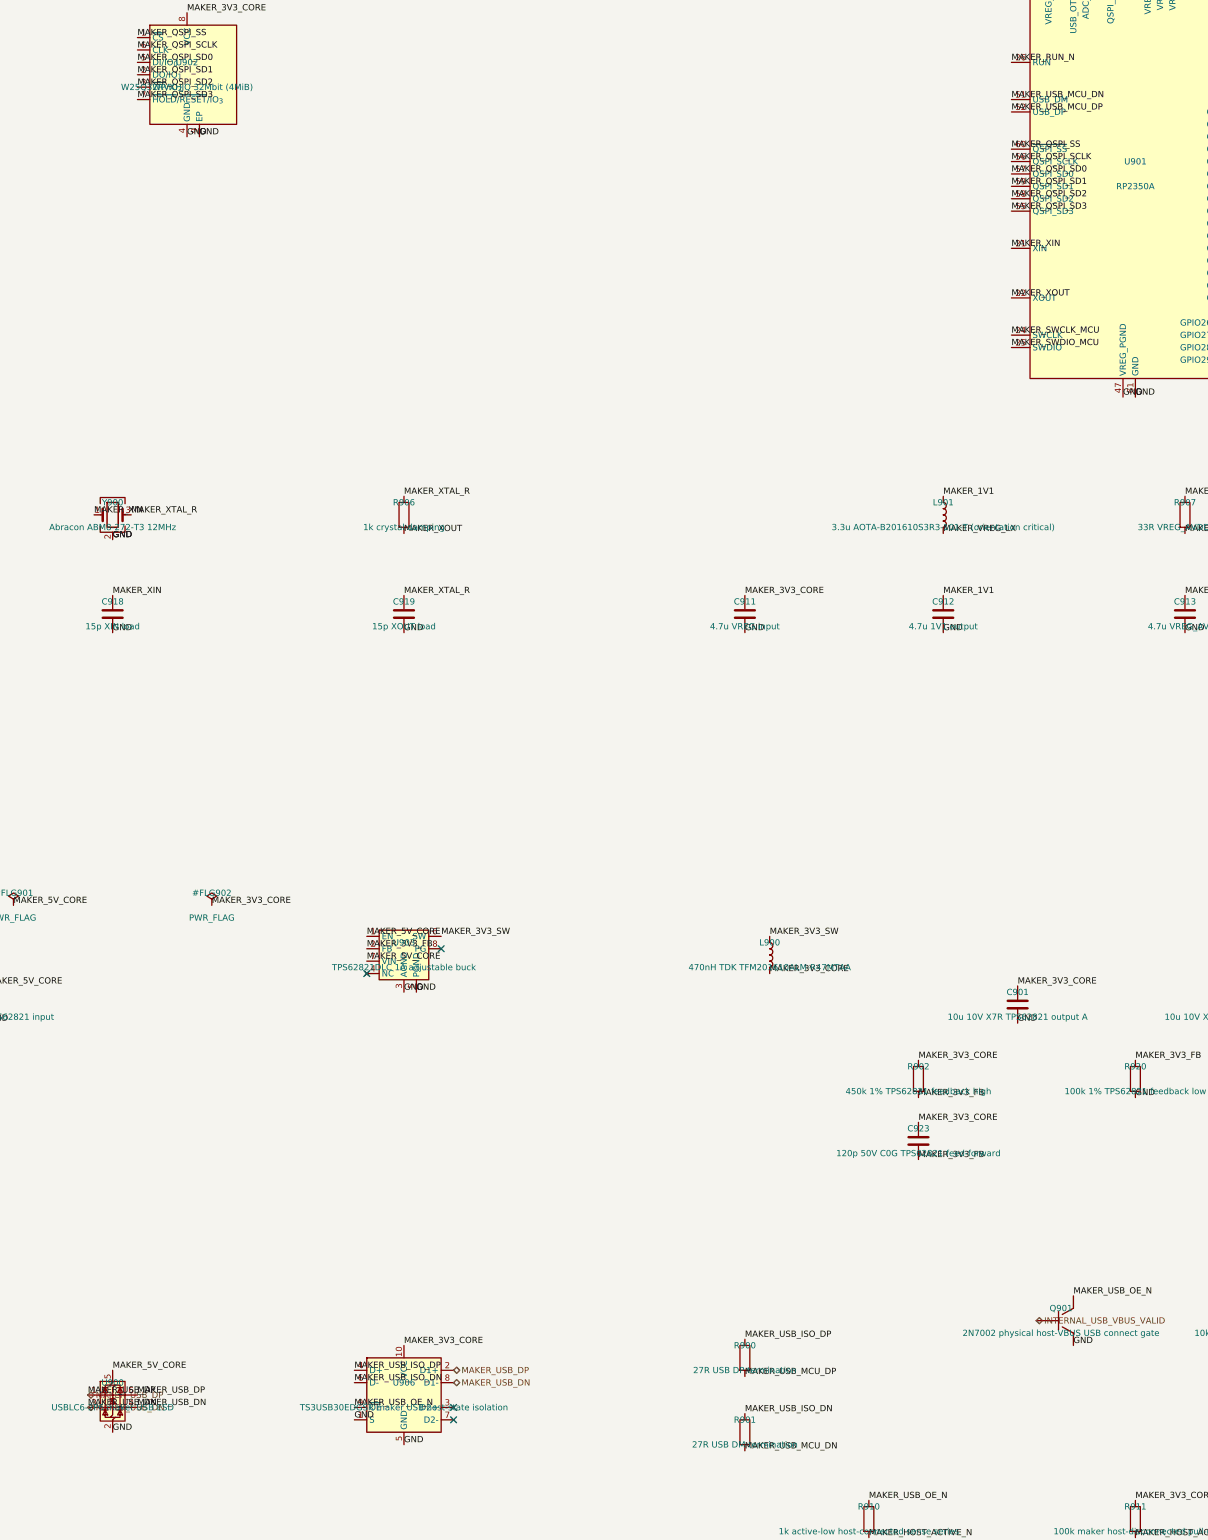
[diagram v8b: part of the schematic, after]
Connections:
- net MAKER_USB_DM renamed MAKER_USB_DN
- net MAKER_USB_DM_MCU renamed MAKER_USB_MCU_DN
- net MAKER_USB_DP_MCU renamed MAKER_USB_MCU_DP
- net MAKER_USB_ISO_DM renamed MAKER_USB_ISO_DN
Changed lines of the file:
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@@
   (effects (font (size 1.27 1.27)) (justify left bottom))
 )
-(label "MAKER_USB_DM_MCU"
+(label "MAKER_USB_MCU_DN"
   (at 274.32 129.54 0)
   (effects (font (size 1.27 1.27)) (justify left bottom))
 )
-(label "MAKER_USB_DP_MCU"
+(label "MAKER_USB_MCU_DP"
   (at 274.32 132.08 0)
   (effects (font (size 1.27 1.27)) (justify left bottom))
@@
   (effects (font (size 1.27 1.27)) (justify left bottom))
 )
-(label "MAKER_USB_DM"
+(label "MAKER_USB_DN"
   (at 85.09 397.51 0)
   (effects (font (size 1.27 1.27)) (justify left bottom))
 )
-(label "MAKER_USB_DM"
+(label "MAKER_USB_DN"
   (at 95.25 397.51 0)
   (effects (font (size 1.27 1.27)) (justify left bottom))
@@
   (effects (font (size 1.27 1.27)) (justify left bottom))
 )
-(hierarchical_label "MAKER_USB_DM"
+(hierarchical_label "MAKER_USB_DN"
   (shape bidirectional)
   (at 85.09 397.51 0)
@@
   (effects (font (size 1.27 1.27)) (justify left bottom))
 )
-(label "MAKER_USB_ISO_DM"
+(label "MAKER_USB_ISO_DN"
   (at 139.7 392.43 0)
   (effects (font (size 1.27 1.27)) (justify left bottom))
 )
 (no_connect (at 160.02 400.05))
-(hierarchical_label "MAKER_USB_DM"
+(hierarchical_label "MAKER_USB_DN"
   (shape bidirectional)
   (at 160.02 392.43 0)
@@
   (effects (font (size 1.27 1.27)) (justify left bottom))
 )
-(label "MAKER_USB_DP_MCU"
+(label "MAKER_USB_MCU_DP"
   (at 219.71 391.16 0)
   (effects (font (size 1.27 1.27)) (justify left bottom))
@@
   )
 )
-(label "MAKER_USB_ISO_DM"
+(label "MAKER_USB_ISO_DN"
   (at 219.71 398.78 0)
   (effects (font (size 1.27 1.27)) (justify left bottom))
 )
-(label "MAKER_USB_DM_MCU"
+(label "MAKER_USB_MCU_DN"
   (at 219.71 406.4 0)
   (effects (font (size 1.27 1.27)) (justify left bottom))
